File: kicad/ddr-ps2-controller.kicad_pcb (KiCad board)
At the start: 2 copper layers, 100 x 40 mm, 71 parts, among them J1 BTN0, J2 BTN1, J3 BTN2, J4 BTN3, J5 ISCP, J6 PS2, J7 BTN4, J8 BTN5/UPSTREAM, Q1 DMN63D8LDW, U1 ATtiny20-MMH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

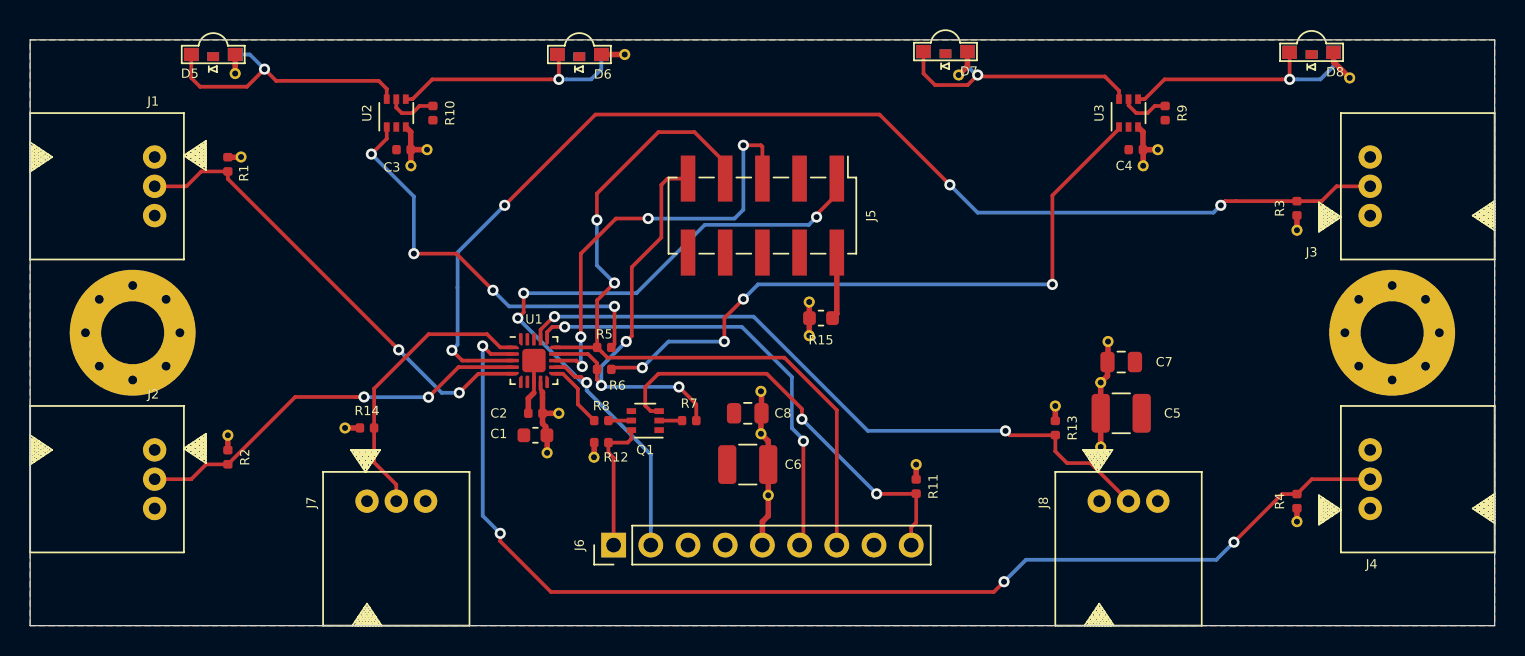
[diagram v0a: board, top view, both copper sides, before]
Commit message: Changed connector to the far cheaper JST-EH
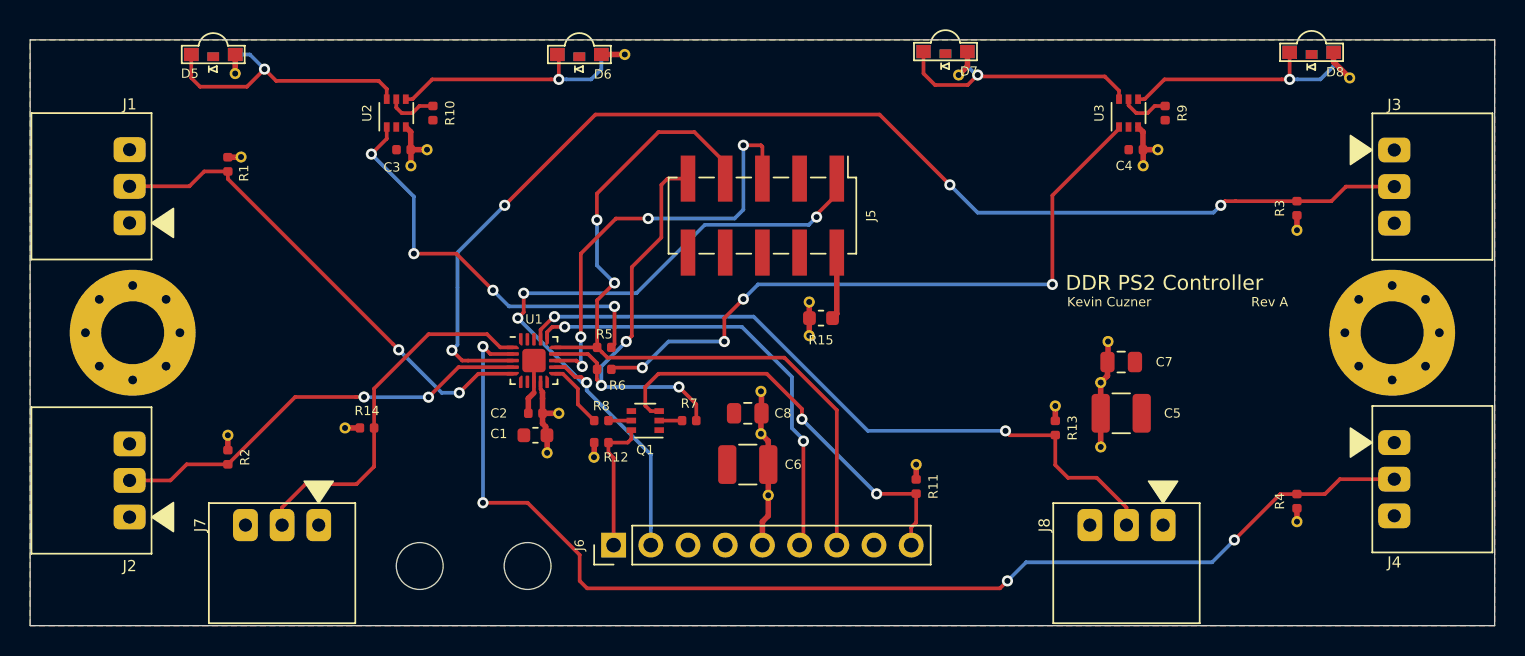
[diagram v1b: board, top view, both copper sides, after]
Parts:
- added REF**: MountingHole_3.2mm_M3, MountingHole:MountingHole_3.2mm_M3, F.Cu at (126.6, 115.9)
- added REF**: MountingHole_3.2mm_M3, MountingHole:MountingHole_3.2mm_M3, F.Cu at (134.0, 115.9)
- J1, J2, J3, J4, J7, J8: footprint ddr-ps2-controller:Molex_35363_2mm_RA -> ddr-ps2-controller:JST_EH_3_RA
- moved J7 7.97 mm to (117.2, 113.1), turned to 0 degrees
- moved J2 1.71 mm to (106.8, 110.1), turned to 270 degrees
- moved J1 1.71 mm to (106.8, 90.0), turned to 270 degrees
- moved J3 1.65 mm to (193.1, 90.0), turned to 90 degrees
- moved J4 1.65 mm to (193.1, 110.0), turned to 90 degrees
- moved J8 1.64 mm to (174.9, 113.1), turned to 0 degrees
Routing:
- net /BTN4: track 19.7 -> 25.3 mm
- net /BTN5_UPSTREAM: track 47.1 -> 48.8 mm
- net /BTN1: track 27.6 -> 29.4 mm
- net /BTN0: track 32.0 -> 33.7 mm
- net /BTN2: track 81.0 -> 82.7 mm
- net /BTN3: track 80.1 -> 81.7 mm
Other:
- board text added: "DDR PS2 Controller"
- board text added: "Kevin Cuzner"
- board text added: "Rev A"

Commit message: Added rounding to the board edges
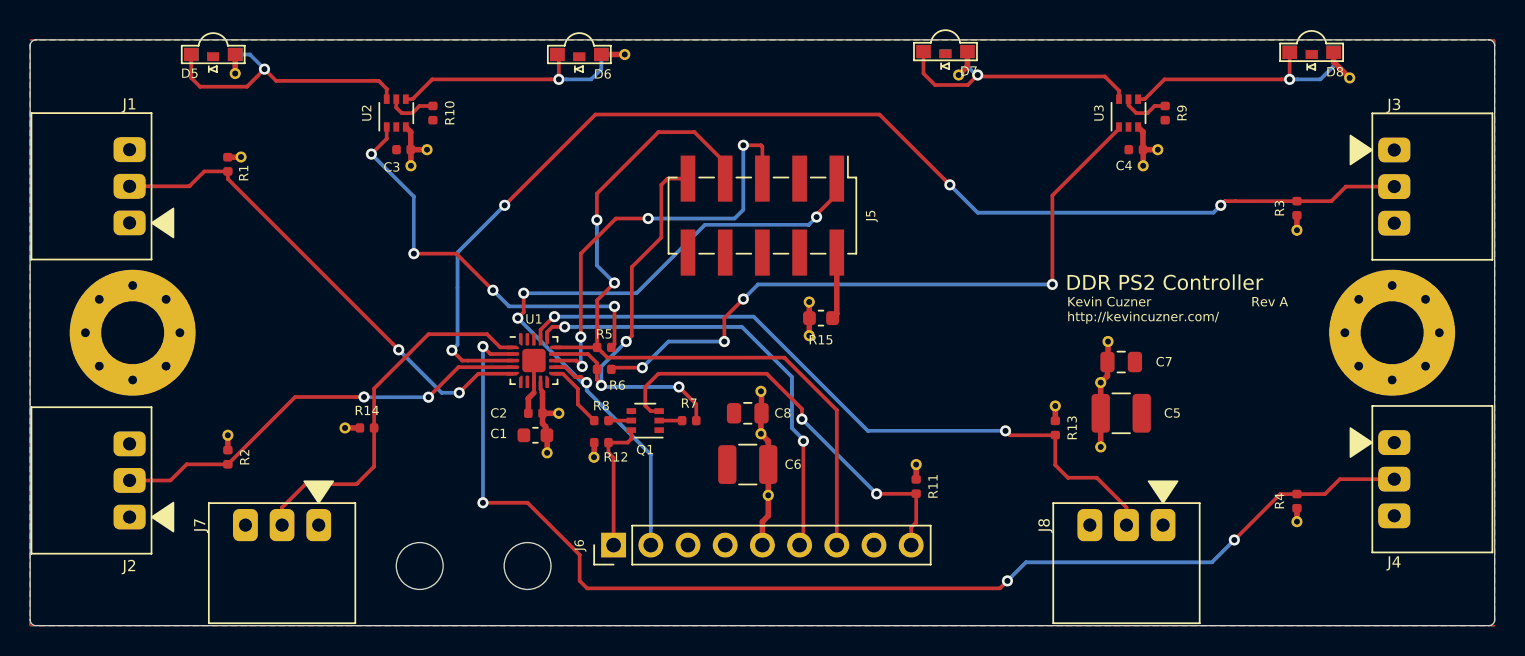
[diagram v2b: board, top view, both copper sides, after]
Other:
- outline, holes or cut-outs redrawn
- board text added: "http://kevincuzner.com/"
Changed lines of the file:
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@@
   (general
     (thickness 1.6)
-    (drawings 9)
+    (drawings 14)
     (tracks 363)
     (zones 0)
@@
     )
   )
+  (gr_arc (start 199.6 80.4) (end 200 80.4) (angle -90) (layer Edge.Cuts) (width 0.05))
+  (gr_arc (start 199.6 119.6) (end 199.6 120) (angle -90) (layer Edge.Cuts) (width 0.05))
+  (gr_arc (start 100.4 119.6) (end 100 119.6) (angle -90) (layer Edge.Cuts) (width 0.05))
+  (gr_arc (start 100.4 80.4) (end 100.4 80) (angle -90) (layer Edge.Cuts) (width 0.05))
+  (gr_text http://kevincuzner.com/ (at 170.8 98.916) (layer F.SilkS)
+    (effects (font (size 0.635 0.635) (thickness 0.15)) (justify left))
+  )
   (gr_text "Rev A" (at 185.9 97.9) (layer F.SilkS)
     (effects (font (size 0.635 0.635) (thickness 0.15)) (justify right))
@@
     (arrow2b (pts (xy 100 71) (xy 101.126504 70.413579)))
   )
-  (gr_line (start 100 120) (end 100 80) (layer Edge.Cuts) (width 0.05))
-  (gr_line (start 200 120) (end 100 120) (layer Edge.Cuts) (width 0.05))
-  (gr_line (start 200 80) (end 200 120) (layer Edge.Cuts) (width 0.05))
-  (gr_line (start 100 80) (end 200 80) (layer Edge.Cuts) (width 0.05))
+  (gr_line (start 100 119.6) (end 100 80.4) (layer Edge.Cuts) (width 0.05))
+  (gr_line (start 199.6 120) (end 100.4 120) (layer Edge.Cuts) (width 0.05))
+  (gr_line (start 200 80.4) (end 200 119.6) (layer Edge.Cuts) (width 0.05))
+  (gr_line (start 100.4 80) (end 199.6 80) (layer Edge.Cuts) (width 0.05))
   (segment (start 153.2 98.9875) (end 153.2125 99) (width 0.381) (layer F.Cu) (net 1))
   (segment (start 153.2 97.9) (end 153.2 98.9875) (width 0.381) (layer F.Cu) (net 1))

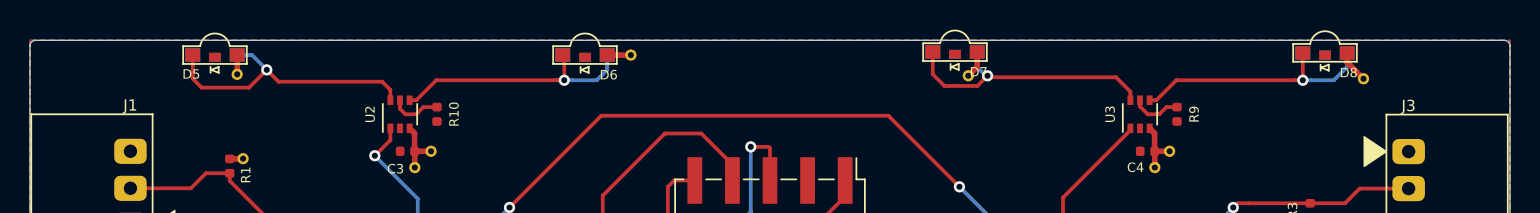
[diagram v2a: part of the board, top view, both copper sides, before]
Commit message: Minor cleanup with LED alignment
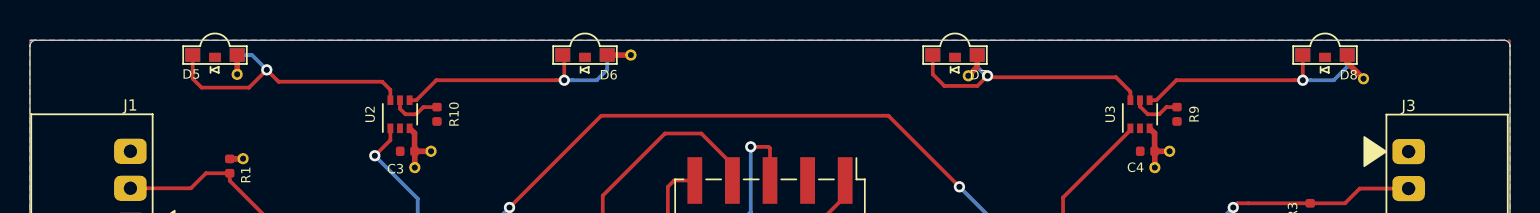
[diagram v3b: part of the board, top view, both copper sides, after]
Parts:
- moved D3 0.20 mm to (162.5, 81.0)
- moved D7 0.20 mm to (162.5, 81.0)
- moved D4 0.15 mm to (187.5, 81.0)
- moved D8 0.15 mm to (187.5, 81.0)
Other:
- outline, holes or cut-outs redrawn
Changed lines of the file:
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@@
   )
   (module ddr-ps2-controller:Wurth_WL-SMSW_LED (layer B.Cu)
-    (at 162.5 80.8 180)
+    (at 162.5 81 180)
     (fp_text reference D3 (at 1.6 -1.35) (layer B.SilkS)
       (effects (font (size 0.635 0.635) (thickness 0.15)) (justify mirror))
@@
   )
   (module ddr-ps2-controller:Wurth_WL-SMSW_LED (layer B.Cu)
-    (at 187.5 80.85 180)
+    (at 187.5 81 180)
     (fp_text reference D4 (at -1.3 -1.45) (layer B.SilkS)
       (effects (font (size 0.635 0.635) (thickness 0.15)) (justify mirror))
@@
   )
   (module ddr-ps2-controller:Wurth_WL-SMSW_LED (layer F.Cu)
-    (at 162.5 80.8)
+    (at 162.5 81)
     (fp_text reference D7 (at 1.6 1.35) (layer F.SilkS)
       (effects (font (size 0.635 0.635) (thickness 0.15)))
@@
   )
   (module ddr-ps2-controller:Wurth_WL-SMSW_LED (layer F.Cu)
-    (at 187.5 80.85)
+    (at 187.5 81)
     (fp_text reference D8 (at 1.6 1.35) (layer F.SilkS)
       (effects (font (size 0.635 0.635) (thickness 0.15)))
@@
   (gr_line (start 199.6 120) (end 100.4 120) (layer Edge.Cuts) (width 0.05))
   (gr_line (start 200 80.4) (end 200 119.6) (layer Edge.Cuts) (width 0.05))
-  (gr_line (start 100.4 80) (end 199.6 80) (layer Edge.Cuts) (width 0.05))
+  (gr_line (start 100 80) (end 199.6 80) (layer Edge.Cuts) (width 0.05))
   (segment (start 153.2 98.9875) (end 153.2125 99) (width 0.381) (layer F.Cu) (net 1))
   (segment (start 153.2 97.9) (end 153.2 98.9875) (width 0.381) (layer F.Cu) (net 1))
@@
   (segment (start 134.985 104.07658) (end 134.958809 104.050389) (width 0.381) (layer F.Cu) (net 1))
   (segment (start 134.985 104.485) (end 134.985 104.07658) (width 0.381) (layer F.Cu) (net 1))
-  (segment (start 189 81.5) (end 190.1 82.6) (width 0.381) (layer F.Cu) (net 1))
-  (segment (start 189 80.85) (end 189 81.5) (width 0.381) (layer F.Cu) (net 1))
   (segment (start 164 81.8) (end 163.4 82.4) (width 0.381) (layer F.Cu) (net 1))
-  (segment (start 164 80.8) (end 164 81.8) (width 0.381) (layer F.Cu) (net 1))
   (segment (start 114 82.3) (end 114 81) (width 0.381) (layer F.Cu) (net 1))
   (segment (start 140.6 81) (end 139 81) (width 0.381) (layer F.Cu) (net 1))
+  (segment (start 164 81.8) (end 164 81) (width 0.381) (layer F.Cu) (net 1))
+  (segment (start 189 81.5) (end 190.1 82.6) (width 0.381) (layer F.Cu) (net 1))
+  (segment (start 189 81) (end 189 81.5) (width 0.381) (layer F.Cu) (net 1))
   (segment (start 134.015 104.485) (end 134.015 105.5) (width 0.381) (layer F.Cu) (net 2))
   (segment (start 134.4 104.1) (end 134.015 104.485) (width 0.381) (layer F.Cu) (net 2))
@@
   (segment (start 111 82.6) (end 111 81) (width 0.254) (layer F.Cu) (net 3))
   (segment (start 111.6 83.2) (end 111 82.6) (width 0.254) (layer F.Cu) (net 3))
+  (segment (start 127.454 82.7) (end 135.561185 82.7) (width 0.254) (layer F.Cu) (net 4))
   (via (at 136.1 82.7) (size 0.762) (drill 0.4064) (layers F.Cu B.Cu) (net 4))
-  (segment (start 125.65 84.05) (end 126.104 84.05) (width 0.254) (layer F.Cu) (net 4))
-  (segment (start 127.454 82.7) (end 135.561185 82.7) (width 0.254) (layer F.Cu) (net 4))
+  (segment (start 136.1 82.7) (end 136.1 81.1) (width 0.254) (layer F.Cu) (net 4))
+  (segment (start 139 82) (end 138.3 82.7) (width 0.254) (layer B.Cu) (net 4))
   (segment (start 126.104 84.05) (end 127.454 82.7) (width 0.254) (layer F.Cu) (net 4))
   (segment (start 135.561185 82.7) (end 136.1 82.7) (width 0.254) (layer F.Cu) (net 4))
-  (segment (start 136.638815 82.7) (end 136.1 82.7) (width 0.254) (layer B.Cu) (net 4))
+  (segment (start 125.65 84.05) (end 126.104 84.05) (width 0.254) (layer F.Cu) (net 4))
+  (segment (start 136.1 81.1) (end 136 81) (width 0.254) (layer F.Cu) (net 4))
   (segment (start 139 81) (end 139 82) (width 0.254) (layer B.Cu) (net 4))
   (segment (start 138.3 82.7) (end 136.638815 82.7) (width 0.254) (layer B.Cu) (net 4))
-  (segment (start 139 82) (end 138.3 82.7) (width 0.254) (layer B.Cu) (net 4))
-  (segment (start 136.1 81.1) (end 136 81) (width 0.254) (layer F.Cu) (net 4))
-  (segment (start 136.1 82.7) (end 136.1 81.1) (width 0.254) (layer F.Cu) (net 4))
+  (segment (start 136.638815 82.7) (end 136.1 82.7) (width 0.254) (layer B.Cu) (net 4))
   (segment (start 174.35 83.471) (end 173.379 82.5) (width 0.254) (layer F.Cu) (net 5))
   (segment (start 174.35 84.05) (end 174.35 83.471) (width 0.254) (layer F.Cu) (net 5))
@@
   (segment (start 173.379 82.5) (end 164.8 82.5) (width 0.254) (layer F.Cu) (net 5))
   (segment (start 164.8 82.5) (end 164.7 82.4) (width 0.254) (layer F.Cu) (net 5))
-  (segment (start 164 81.8) (end 164 80.85) (width 0.254) (layer B.Cu) (net 5))
   (segment (start 164.7 82.4) (end 164.6 82.4) (width 0.254) (layer B.Cu) (net 5))
   (segment (start 164.6 82.4) (end 164 81.8) (width 0.254) (layer B.Cu) (net 5))
-  (segment (start 161 82.3) (end 161 80.8) (width 0.254) (layer F.Cu) (net 5))
   (segment (start 161.785801 83.085801) (end 161 82.3) (width 0.254) (layer F.Cu) (net 5))
   (segment (start 164.7 82.4) (end 164.014199 83.085801) (width 0.254) (layer F.Cu) (net 5))
   (segment (start 164.014199 83.085801) (end 161.785801 83.085801) (width 0.254) (layer F.Cu) (net 5))
+  (segment (start 164 81.8) (end 164 81) (width 0.254) (layer B.Cu) (net 5))
+  (segment (start 161 82.3) (end 161 81) (width 0.254) (layer F.Cu) (net 5))
   (segment (start 175.65 84.05) (end 176.104 84.05) (width 0.254) (layer F.Cu) (net 6))
   (segment (start 177.454 82.7) (end 185.461185 82.7) (width 0.254) (layer F.Cu) (net 6))
